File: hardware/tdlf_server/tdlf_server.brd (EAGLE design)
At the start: 29.5 x 100 mm, 34 parts, among them IC4 DAC8564, IC6 OPA4171

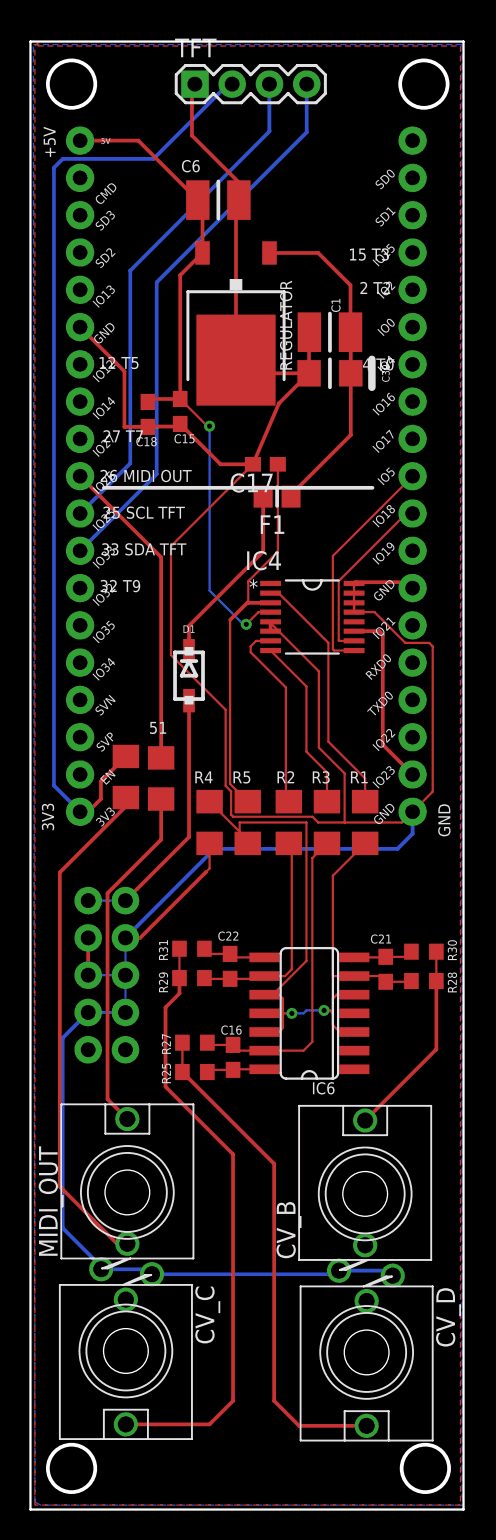
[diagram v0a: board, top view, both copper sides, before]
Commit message: Moving to TRS for midi and three CV outputs
For future use with physical interfaces sending sensor data via UDP to the server.
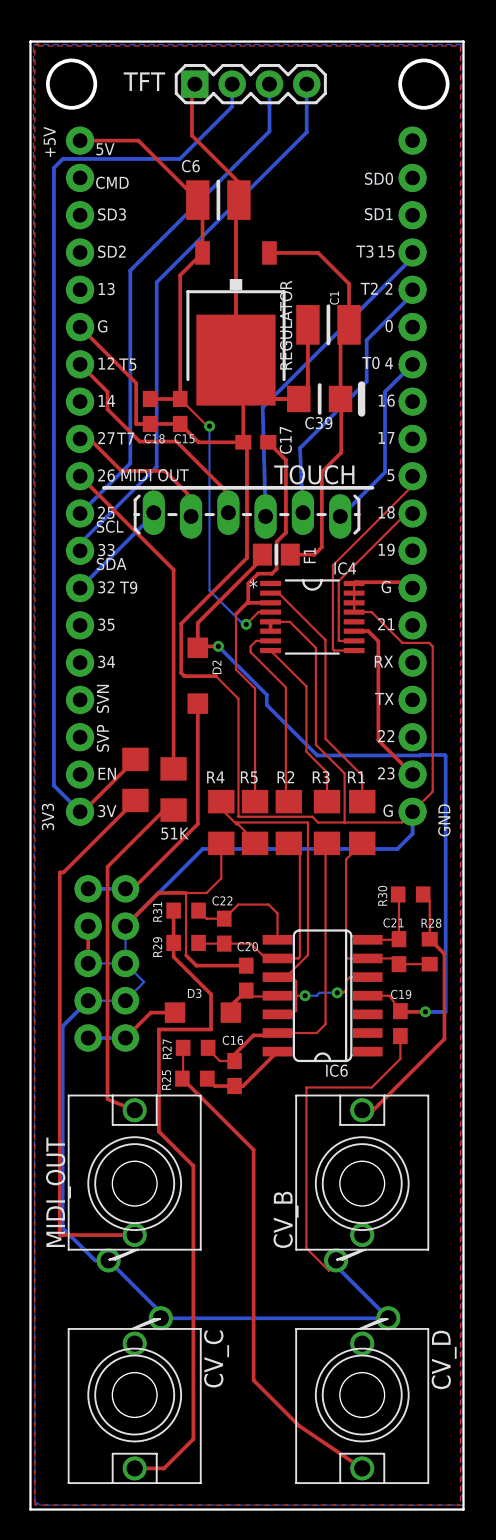
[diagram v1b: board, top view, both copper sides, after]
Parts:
- removed 51: (no value), SparkFun-Resistors:1206
- removed D1: 1N5819HW, parts_aman:SOD123
- added 51K: (no value), SparkFun-Resistors:1206
- added C19, C20: 100n, rcl:C0603
- added D2: B0450, diode:SOD123
- added D3: B0540, diode:SOD123
- added TOUCH: (no value), SparkFun-Connectors:1X06_LOCK_LONGPADS
- moved R30 4.00 mm to (25.9, 41.9)
- moved F1 3.95 mm to (16.8, 65.0)
- moved CV_C 3.06 mm to (7.10, 7.80)
- moved CV_D 2.92 mm to (22.6, 7.80)
- moved R31 2.63 mm to (10.6, 40.8)
- moved C22 2.43 mm to (13.2, 39.4)
- moved R29 2.43 mm to (10.6, 38.6)
- moved R28 2.04 mm to (27.2, 38.0), turned to 270 degrees
- moved C39 1.88 mm to (19.7, 75.7)
- moved C17 1.63 mm to (15.3, 72.7)
- moved C21 1.50 mm to (25.1, 38.0)
- moved IC6 1.50 mm to (19.9, 35.0)
- moved C16 1.10 mm to (13.9, 29.7)
- moved PWR_10 0.80 mm to (5.20, 37.2)
- moved R4 0.80 mm to (13.0, 46.8)
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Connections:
- removed net +12: D1.+, PWR_10.10, PWR_10.9
- removed net ADC4: ESP32.7
- removed net D5: ESP32.26
- removed net D8: ESP32.24
- removed net MISO: ESP32.13
- removed net N$3: ESP32.11
- removed net N$47: D1.-, F1.2
- removed net SPI_SS: ESP32.23
- new net N$1: D3.C, PWR_10.1, PWR_10.2
- new net N$4: D2.A, PWR_10.10, PWR_10.9
- new net TOUCH0: ESP32.26, TOUCH.1
- new net TOUCH2: ESP32.24, TOUCH.2
- new net TOUCH3: ESP32.23, TOUCH.3
- new net TOUCH5: ESP32.13, TOUCH.4
- new net TOUCH7: ESP32.11, TOUCH.5
- new net TOUCH9: ESP32.7, TOUCH.6
- net DAC2: now also 51K.1; no longer 51.1
- net GND: now also C19.2, C20.1
- net PIN27: now also 51K.2; no longer 51.2
- net V+: now also C19.1, D2.C, F1.2
- net V-: now also C20.2, D3.A
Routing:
- net V+: track 0.00 -> 51.9 mm, vias 0 -> 2
- net GND: track 224.1 -> 264.1 mm
- net TOUCH3: track 0.00 -> 22.2 mm
- net TOUCH2: track 0.00 -> 18.4 mm
- net +12: track 18.0 -> 0.00 mm
- net N$4: track 0.00 -> 17.5 mm
- net TOUCH5: track 0.00 -> 15.7 mm
- net N$47: track 12.6 -> 0.00 mm
- net TOUCH0: track 0.00 -> 12.4 mm
- net TOUCH7: track 0.00 -> 10.6 mm
- net TOUCH9: track 0.00 -> 7.19 mm
- net N$1: track 0.00 -> 6.64 mm
- net N$55: track 41.1 -> 46.4 mm
- net +12V: track 22.5 -> 27.4 mm
- net N$63: track 13.5 -> 18.1 mm
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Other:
- outline, holes or cut-outs redrawn
- board text added: "+12V"
- board text added: "-12V"
- board text added: "MIDI OUT"
- board text added: "SCL"
- board text added: "SDA"
- board text added: "T0"
- board text added: "T2"
- board text added: "T3"
- board text added: "T5"
- board text added: "T7"
- board text added: "T9"
- board text removed: "12 T5"
- board text removed: "15 T3"
- board text removed: "2 T2"
- board text removed: "25 SCL TFT"
- board text removed: "26 MIDI OUT"
- board text removed: "27 T7"
- board text removed: "32 T9"
- board text removed: "33 SDA TFT"
- board text removed: "4 T0"

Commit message: Now with 3 CV outputs !
Midi TRS out works
CV out : the hardware works but the code needs to be implemented. Help needed :).
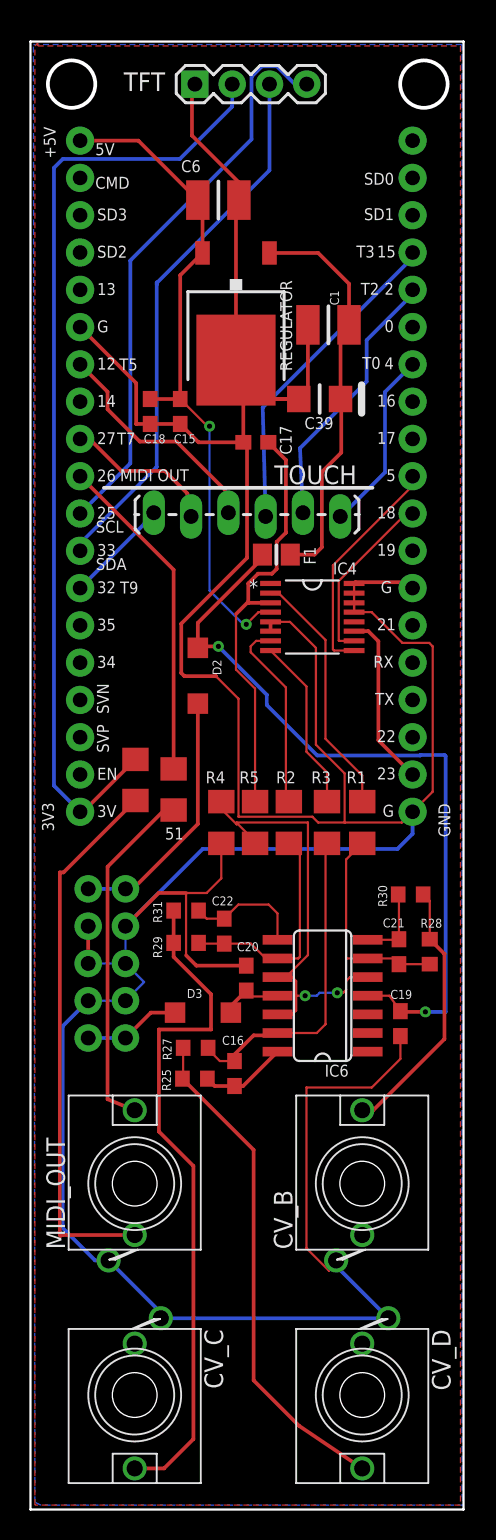
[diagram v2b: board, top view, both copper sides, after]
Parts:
- renumbered 51K to 51
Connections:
- net IO25: now also TFT.4; no longer TFT.3
- net IO33: now also TFT.3; no longer TFT.4
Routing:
- net IO25: track 34.6 -> 39.2 mm
- net IO33: track 38.2 -> 37.2 mm
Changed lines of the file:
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@@
 </layers>
 <board>
-<fusionsync huburn="a.cGVyc29uYWw6dWUyYTYyMmQz" projecturn="a.cGVyc29uYWw6dWUyYTYyMmQzIzIwMjAwMTA4MjUzMTkwODgx" f3durn="urn:adsk.wipprod:dm.lineage:EJ7CIL_8QPSL4HfMM387xA" pcbguid="" lastpulledtime="" lastsyncedchangeguid="" latestrevisionid="7d571e40-2c82-453b-b189-2d8ddc5c869f" lastsyncedrevisionid="7d571e40-2c82-453b-b189-2d8ddc5c869f" lastboardhashguid="83bfc7fe-6b66-0ea3-aab0-548db4954436" lastpushedtime="2021-06-20T17:21:24Z" linktopcb3d="false"/>
+<fusionsync huburn="a.cGVyc29uYWw6dWUyYTYyMmQz" projecturn="a.cGVyc29uYWw6dWUyYTYyMmQzIzIwMjAwMTA4MjUzMTkwODgx" f3durn="urn:adsk.wipprod:dm.lineage:EJ7CIL_8QPSL4HfMM387xA" pcbguid="" lastpulledtime="" lastsyncedchangeguid="" latestrevisionid="7d571e40-2c82-453b-b189-2d8ddc5c869f" lastsyncedrevisionid="7d571e40-2c82-453b-b189-2d8ddc5c869f" lastboardhashguid="83bfc7fe-6b66-0ea3-aab0-548db4954436" lastpushedtime="2021-06-20T17:21:24Z" linktopcb3d="true"/>
 <plain>
 <wire x1="0" y1="0" x2="0" y2="100" width="0.1524" layer="20"/>
@@
 <attribute name="VALUE" x="5.407" y="49.9" size="0.6096" layer="27" font="vector" ratio="20" rot="R270" align="top-center"/>
 </element>
-<element name="51K" library="SparkFun-Resistors" library_urn="urn:adsk.eagle:library:532" package="1206" package3d_urn="urn:adsk.eagle:package:39654/1" value=" " x="9.75" y="49.05" smashed="yes" rot="R270">
+<element name="51" library="SparkFun-Resistors" library_urn="urn:adsk.eagle:library:532" package="1206" package3d_urn="urn:adsk.eagle:package:39654/1" value=" " x="9.75" y="49.05" smashed="yes" rot="R270">
 <attribute name="NAME" x="9.8" y="45.643" size="0.8128" layer="25" ratio="20" align="bottom-center"/>
 <attribute name="PROD_ID" value=" " x="9.75" y="49.05" size="1.778" layer="27" rot="R270" display="off"/>
@@
 </signal>
 <signal name="PIN27">
-<contactref element="51K" pad="2"/>
+<contactref element="51" pad="2"/>
 <contactref element="MIDI_OUT" pad="P$1"/>
 <wire x1="5.2508" y1="43.7850125" x2="9.1157875" y2="47.65" width="0.254" layer="1"/>
@@
 <signal name="IO33">
 <contactref element="ESP32" pad="8"/>
-<contactref element="TFT" pad="4"/>
-<wire x1="18.82" y1="97.1" x2="18.82" y2="93.82" width="0.254" layer="16"/>
 <wire x1="8.6" y1="71.03" x2="3.38" y2="65.81" width="0.254" layer="16"/>
 <wire x1="3.38" y1="65.81" x2="3.38" y2="65.31" width="0.254" layer="16"/>
-<wire x1="18.82" y1="93.82" x2="8.6" y2="83.6" width="0.254" layer="16"/>
-<wire x1="8.6" y1="83.6" x2="8.6" y2="71.03" width="0.254" layer="16"/>
+<wire x1="8.6" y1="83.6" x2="8.6" y2="83.55" width="0.254" layer="16"/>
+<contactref element="TFT" pad="3"/>
+<wire x1="8.6" y1="83.45" x2="8.6" y2="71.03" width="0.254" layer="16"/>
+<wire x1="16.28" y1="97.1" x2="16.28" y2="91.23" width="0.254" layer="16"/>
+<wire x1="8.6" y1="83.55" x2="8.6" y2="83.45" width="0.254" layer="16"/>
+<wire x1="16.28" y1="91.23" x2="8.6" y2="83.55" width="0.254" layer="16"/>
 </signal>
 <signal name="SPI_CLK">
@@
 <signal name="IO25">
 <contactref element="ESP32" pad="9"/>
-<contactref element="TFT" pad="3"/>
-<wire x1="16.28" y1="97.1" x2="16.28" y2="93.88" width="0.254" layer="16"/>
-<wire x1="6.8" y1="71.27" x2="3.38" y2="67.85" width="0.254" layer="16"/>
-<wire x1="16.28" y1="93.88" x2="6.8" y2="84.4" width="0.254" layer="16"/>
-<wire x1="6.8" y1="84.4" x2="6.8" y2="71.27" width="0.254" layer="16"/>
+<wire x1="3.38" y1="67.85" x2="6.8" y2="71.27" width="0.254" layer="16"/>
+<contactref element="TFT" pad="4"/>
+<wire x1="15.0608" y1="97.6050125" x2="15.7749875" y2="98.3192" width="0.254" layer="16"/>
+<wire x1="15.7749875" y1="98.3192" x2="16.7850125" y2="98.3192" width="0.254" layer="16"/>
+<wire x1="6.8" y1="85.08" x2="15.0608" y2="93.3408" width="0.254" layer="16"/>
+<wire x1="15.0608" y1="93.3408" x2="15.0608" y2="97.6050125" width="0.254" layer="16"/>
+<wire x1="16.7850125" y1="98.3192" x2="18.0042125" y2="97.1" width="0.254" layer="16"/>
+<wire x1="18.0042125" y1="97.1" x2="18.82" y2="97.1" width="0.254" layer="16"/>
+<wire x1="6.8" y1="71.27" x2="6.8" y2="85.08" width="0.254" layer="16"/>
 </signal>
 <signal name="DAC2">
 <contactref element="ESP32" pad="10"/>
-<contactref element="51K" pad="1"/>
+<contactref element="51" pad="1"/>
 <wire x1="3.38" y1="70.39" x2="9.75" y2="64.02" width="0.254" layer="1"/>
 <wire x1="9.75" y1="64.02" x2="9.75" y2="50.45" width="0.254" layer="1"/>

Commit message: Version 0.5 ready for CV outputs
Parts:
- removed C15: 3.3u, rcl:C0603
- removed C17: 220n, rcl:C0603
- removed C18: 100n, rcl:C0603
- removed IC4: DAC8564, og-dac:SOP65P640X110-16N
- removed R4, R5: 47k, rcl:R1206
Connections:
- removed net +3V3: IC4.12
- removed net CH_A: IC4.1
- removed net CH_B: IC4.2, R1.1
- removed net CH_C: IC4.7, R2.1
- removed net CH_D: IC4.8, R3.1
- removed net N$55: CV_C.P$1, R29.1, R31.1
- removed net N$58: CV_D.P$1, R25.1, R27.1
- removed net SPI_MOSI: ESP32.37, IC4.11
- removed net VREF: C17.1, IC4.3, R5.2
- removed net VREF/2: IC6.10, IC6.12, IC6.5, R4.2, R5.1
- removed net VSPI_CLK: ESP32.30, IC4.10
- removed net VSPI_SS: ESP32.29, IC4.9
- new net DAC_B: ESP32.29, IC6.5
- new net DAC_C: ESP32.37, IC6.10
- new net DAC_D: ESP32.30, IC6.12
- new net N$3: CV_C.P$1, R31.1
- new net N$5: CV_D.P$1, R25.1
- net +5V: no longer C15.1, C18.1, IC4.4
- net GND: now also R1.1, R2.1, R3.1; no longer C15.2, C17.2, C18.2, IC4.13, IC4.14, IC4.15, IC4.16, IC4.5, IC4.6, R4.1
- net N$50: now also R28.1
- net N$51: now also R29.1
- net N$52: now also R27.1
- net N$63: no longer R28.1
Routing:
- net DAC_D: track 0.00 -> 48.6 mm
- net N$3: track 0.00 -> 48.3 mm
- net N$55: track 46.4 -> 0.00 mm
- net DAC_B: track 0.00 -> 40.3 mm, vias 0 -> 2
- net N$58: track 34.3 -> 0.00 mm
- net +5V: track 45.6 -> 13.4 mm, vias 2 -> 0
- net N$5: track 0.00 -> 31.7 mm
- net VREF/2: track 31.1 -> 0.00 mm, vias 2 -> 0
- net VREF: track 29.1 -> 0.00 mm
- net GND: track 264.1 -> 236.3 mm, vias 0 -> 1
- net DAC_C: track 0.00 -> 26.0 mm
- net CH_B: track 17.1 -> 0.00 mm
- net VSPI_SS: track 15.5 -> 0.00 mm
- net CH_C: track 13.2 -> 0.00 mm
- net VSPI_CLK: track 12.0 -> 0.00 mm
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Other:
- board text added: "tdlf v 0.5 acastonguay@artengine.ca"
- board text removed: "tdlf v 0.4 acastonguay@artengine.ca"
